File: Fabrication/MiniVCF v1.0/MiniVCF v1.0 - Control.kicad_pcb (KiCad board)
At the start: 2 copper layers, 30 x 102.5 mm, 28 parts, among them J10 CV2, J11 CTRL_PANEL_CONN2, J3 AudioIn, J4 CV1, J5 AudioOut, J6 CONN_PWR1, J9 CTRL_PANEL_CONN

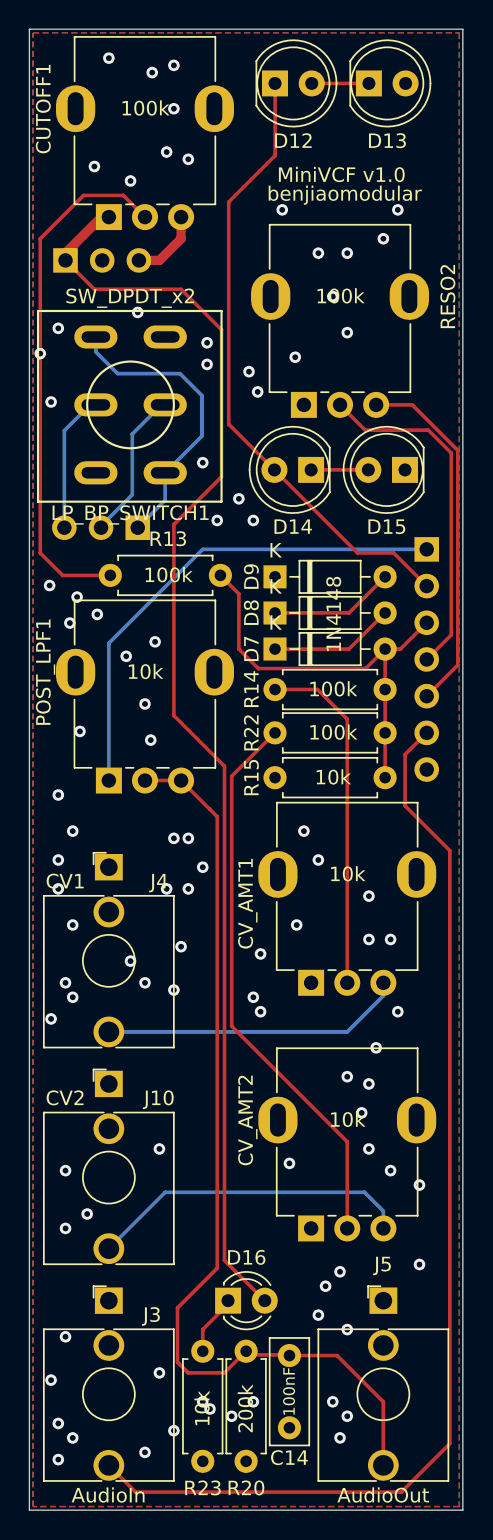
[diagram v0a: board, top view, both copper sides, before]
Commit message: Added a lock hole on control and main board
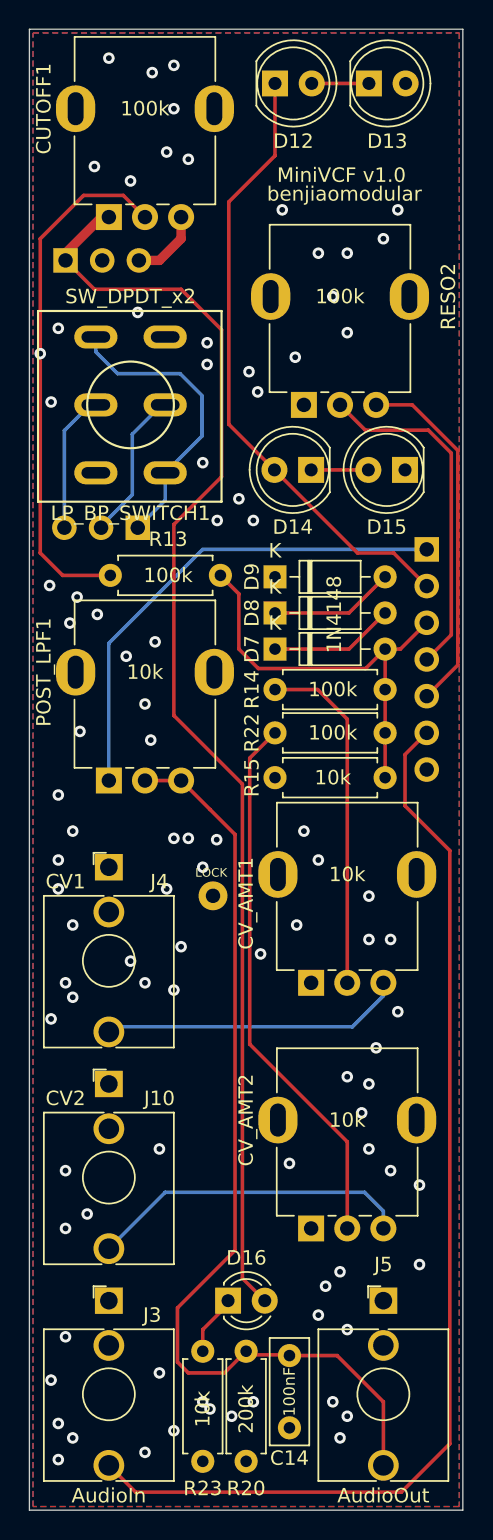
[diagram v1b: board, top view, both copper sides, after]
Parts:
- added REF**: Wire_1mm, benjiaomodular:Wire_1mm, F.Cu at (84.7, 113.0)
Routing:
- net Net-(CV_AMT2-Pad2): track 38.9 -> 37.8 mm
- net Net-(C14-Pad2): track 66.0 -> 67.0 mm
- net GND1: vias 94 -> 92
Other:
- board text added: "LOCK"
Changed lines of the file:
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@@
   (general
     (thickness 1.6)
-    (drawings 8)
-    (tracks 207)
+    (drawings 14)
+    (tracks 206)
     (zones 0)
-    (modules 28)
+    (modules 29)
     (nets 24)
   )
@@
     (add_net POS12V_1)
   )
+  (module benjiaomodular:Wire_1mm (layer F.Cu)
+    (at 84.709 113.03)
+    (fp_text reference REF** (at 0 -2) (layer F.SilkS) hide
+      (effects (font (size 1 1) (thickness 0.15)))
+    )
+    (fp_text value Wire_1mm (at 0 1.5) (layer F.Fab)
+      (effects (font (size 1 1) (thickness 0.15)))
+    )
+    (pad 1 thru_hole circle (at 0 -0.05) (size 2 2) (drill 1) (layers *.Cu *.Mask))
+  )
   (module benjiaomodular:ToggleSwitch_MTS-202_DPDT (layer F.Cu)
     (at 79 79 180)
@@
       (net 4 GND1))
   )
+  (gr_text LOCK (at 84.582 111.379) (layer B.SilkS)
+    (effects (font (size 0.6 0.6) (thickness 0.15)) (justify mirror))
+  )
+  (gr_text LOCK (at 84.582 111.379) (layer F.SilkS)
+    (effects (font (size 0.6 0.6) (thickness 0.15)))
+  )
+  (dimension 12.7 (width 0.15) (layer Dwgs.User)
+    (gr_text "12.700 mm" (at 78.359 117.632) (layer Dwgs.User)
+      (effects (font (size 1 1) (thickness 0.15)))
+    )
+    (feature1 (pts (xy 84.709 113.538) (xy 84.709 116.918421)))
+    (feature2 (pts (xy 72.009 113.538) (xy 72.009 116.918421)))
+    (crossbar (pts (xy 72.009 116.332) (xy 84.709 116.332)))
+    (arrow1a (pts (xy 84.709 116.332) (xy 83.582496 116.918421)))
+    (arrow1b (pts (xy 84.709 116.332) (xy 83.582496 115.745579)))
+    (arrow2a (pts (xy 72.009 116.332) (xy 73.135504 116.918421)))
+    (arrow2b (pts (xy 72.009 116.332) (xy 73.135504 115.745579)))
+  )
+  (dimension 15 (width 0.15) (layer Dwgs.User)
+    (gr_text "15.000 mm" (at 79.5 160.2) (layer Dwgs.User)
+      (effects (font (size 1 1) (thickness 0.15)))
+    )
+    (feature1 (pts (xy 87 141) (xy 87 159.486421)))
+    (feature2 (pts (xy 72 141) (xy 72 159.486421)))
+    (crossbar (pts (xy 72 158.9) (xy 87 158.9)))
+    (arrow1a (pts (xy 87 158.9) (xy 85.873496 159.486421)))
+    (arrow1b (pts (xy 87 158.9) (xy 85.873496 158.313579)))
+    (arrow2a (pts (xy 72 158.9) (xy 73.126504 159.486421)))
+    (arrow2b (pts (xy 72 158.9) (xy 73.126504 158.313579)))
+  )
   (dimension 10.5 (width 0.15) (layer Dwgs.User)
     (gr_text "10.500 mm" (at 96.75 139.5) (layer Dwgs.User)
@@
     (arrow2b (pts (xy 91.5 138.2) (xy 92.626504 137.613579)))
   )
+  (dimension 5.500036 (width 0.15) (layer Dwgs.User)
+    (gr_text "5.500 mm" (at 99.207077 159.293852 359.7916526) (layer Dwgs.User)
+      (effects (font (size 1 1) (thickness 0.15)))
+    )
+    (feature1 (pts (xy 102 147.5) (xy 101.959672 158.590277)))
+    (feature2 (pts (xy 96.5 147.48) (xy 96.459672 158.570277)))
+    (crossbar (pts (xy 96.461804 157.983861) (xy 101.961804 158.003861)))
+    (arrow1a (pts (xy 101.961804 158.003861) (xy 100.833175 158.586182)))
+    (arrow1b (pts (xy 101.961804 158.003861) (xy 100.83744 157.413348)))
+    (arrow2a (pts (xy 96.461804 157.983861) (xy 97.586168 158.574374)))
+    (arrow2b (pts (xy 96.461804 157.983861) (xy 97.590433 157.40154)))
+  )
   (dimension 7 (width 0.15) (layer Dwgs.User)
     (gr_text "7.000 mm" (at 75.5 84) (layer Dwgs.User)
@@
     (arrow2a (pts (xy 72 82.7) (xy 73.126504 83.286421)))
     (arrow2b (pts (xy 72 82.7) (xy 73.126504 82.113579)))
+  )
+  (dimension 5.5 (width 0.15) (layer Dwgs.User)
+    (gr_text "5.500 mm" (at 74.75 163.8) (layer Dwgs.User)
+      (effects (font (size 1 1) (thickness 0.15)))
+    )
+    (feature1 (pts (xy 72 66) (xy 72 163.086421)))
+    (feature2 (pts (xy 77.5 66) (xy 77.5 163.086421)))
+    (crossbar (pts (xy 77.5 162.5) (xy 72 162.5)))
+    (arrow1a (pts (xy 72 162.5) (xy 73.126504 161.913579)))
+    (arrow1b (pts (xy 72 162.5) (xy 73.126504 163.086421)))
+    (arrow2a (pts (xy 77.5 162.5) (xy 76.373496 161.913579)))
+    (arrow2b (pts (xy 77.5 162.5) (xy 76.373496 163.086421)))
   )
   (gr_text benjiaomodular (at 93.8 64.4) (layer F.SilkS)
@@
   (via (at 82 119.5) (size 0.8) (drill 0.4) (layers F.Cu B.Cu) (net 4))
   (via (at 82.5 116.5) (size 0.8) (drill 0.4) (layers F.Cu B.Cu) (net 4))
-  (via (at 83 112.5) (size 0.8) (drill 0.4) (layers F.Cu B.Cu) (net 4))
+  (via (at 84.963 109.093) (size 0.8) (drill 0.4) (layers F.Cu B.Cu) (net 4))
   (via (at 84 111) (size 0.8) (drill 0.4) (layers F.Cu B.Cu) (net 4))
   (via (at 83 109) (size 0.8) (drill 0.4) (layers F.Cu B.Cu) (net 4))
@@
   (via (at 90.5 115) (size 0.8) (drill 0.4) (layers F.Cu B.Cu) (net 4))
   (via (at 88 117) (size 0.8) (drill 0.4) (layers F.Cu B.Cu) (net 4))
-  (via (at 87.5 120) (size 0.8) (drill 0.4) (layers F.Cu B.Cu) (net 4))
-  (via (at 88 121) (size 0.8) (drill 0.4) (layers F.Cu B.Cu) (net 4))
   (via (at 95.5 116) (size 0.8) (drill 0.4) (layers F.Cu B.Cu) (net 4))
   (via (at 95.5 113) (size 0.8) (drill 0.4) (layers F.Cu B.Cu) (net 4))
@@
   (segment (start 79.58 69) (end 81 69) (width 0.65) (layer F.Cu) (net 5))
   (segment (start 81 69) (end 82.5 67.5) (width 0.65) (layer F.Cu) (net 5))
-  (segment (start 85.3 83.97745) (end 85.3 73.8) (width 0.25) (layer F.Cu) (net 6))
-  (segment (start 85.5 138.21) (end 85.5 104) (width 0.25) (layer F.Cu) (net 6))
-  (segment (start 88.29 141) (end 85.5 138.21) (width 0.25) (layer F.Cu) (net 6) (status 10))
-  (segment (start 82.5 71) (end 76.5 71) (width 0.25) (layer F.Cu) (net 6))
-  (segment (start 85.5 104) (end 82 100.5) (width 0.25) (layer F.Cu) (net 6))
-  (segment (start 82 100.5) (end 82 87.27745) (width 0.25) (layer F.Cu) (net 6))
-  (segment (start 82 87.27745) (end 85.3 83.97745) (width 0.25) (layer F.Cu) (net 6))
-  (segment (start 85.3 73.8) (end 82.5 71) (width 0.25) (layer F.Cu) (net 6))
-  (segment (start 76.5 71) (end 74.5 69) (width 0.25) (layer F.Cu) (net 6) (status 20))
   (segment (start 74.5 68.5) (end 74.5 69) (width 0.65) (layer F.Cu) (net 6))
   (segment (start 77.5 66) (end 77 66) (width 0.65) (layer F.Cu) (net 6))
   (segment (start 77 66) (end 74.5 68.5) (width 0.65) (layer F.Cu) (net 6))
+  (segment (start 76.5 71) (end 74.5 69) (width 0.25) (layer F.Cu) (net 6))
+  (segment (start 85.3 73.8) (end 82.5 71) (width 0.25) (layer F.Cu) (net 6))
+  (segment (start 86.741 139.451) (end 86.741 105.241) (width 0.25) (layer F.Cu) (net 6))
+  (segment (start 88.29 141) (end 86.741 139.451) (width 0.25) (layer F.Cu) (net 6))
+  (segment (start 82.5 71) (end 76.5 71) (width 0.25) (layer F.Cu) (net 6))
+  (segment (start 82 87.27745) (end 85.3 83.97745) (width 0.25) (layer F.Cu) (net 6))
+  (segment (start 85.3 83.97745) (end 85.3 73.8) (width 0.25) (layer F.Cu) (net 6))
+  (segment (start 86.741 105.241) (end 82 100.5) (width 0.25) (layer F.Cu) (net 6))
+  (segment (start 82 100.5) (end 82 87.27745) (width 0.25) (layer F.Cu) (net 6))
   (segment (start 101.64999 97.01001) (end 99.5 99.16) (width 0.25) (layer F.Cu) (net 7) (status 20))
   (segment (start 96 79) (end 98.5 79) (width 0.25) (layer F.Cu) (net 7) (status 10))
@@
   (segment (start 89 98.7) (end 91.95 98.7) (width 0.25) (layer F.Cu) (net 9))
   (segment (start 91.95 98.7) (end 94 100.75) (width 0.25) (layer F.Cu) (net 9))
+  (segment (start 77.853 122.047) (end 94.353 122.047) (width 0.25) (layer B.Cu) (net 10))
+  (segment (start 77.5 122.4) (end 77.853 122.047) (width 0.25) (layer B.Cu) (net 10))
+  (segment (start 94.353 122.047) (end 96.5 119.9) (width 0.25) (layer B.Cu) (net 10))
   (segment (start 96.5 119.9) (end 96.5 119) (width 0.25) (layer B.Cu) (net 10))
-  (segment (start 77.5 122.4) (end 94 122.4) (width 0.25) (layer B.Cu) (net 10))
-  (segment (start 94 122.4) (end 96.5 119.9) (width 0.25) (layer B.Cu) (net 10))
   (segment (start 94 130) (end 94 136) (width 0.25) (layer F.Cu) (net 11))
-  (segment (start 86 122) (end 94 130) (width 0.25) (layer F.Cu) (net 11))
-  (segment (start 89 101.7) (end 86 104.7) (width 0.25) (layer F.Cu) (net 11))
-  (segment (start 86 104.7) (end 86 122) (width 0.25) (layer F.Cu) (net 11))
+  (segment (start 87.249 123.249) (end 94 130) (width 0.25) (layer F.Cu) (net 11))
+  (segment (start 89 101.7) (end 87.249 103.451) (width 0.25) (layer F.Cu) (net 11))
+  (segment (start 87.249 103.451) (end 87.249 123.249) (width 0.25) (layer F.Cu) (net 11))
   (segment (start 96.5 134.8) (end 96.5 136) (width 0.25) (layer B.Cu) (net 12))
   (segment (start 95.2 133.5) (end 96.5 134.8) (width 0.25) (layer B.Cu) (net 12))
@@
   (segment (start 87.25 144.75) (end 89.95 144.75) (width 0.25) (layer F.Cu) (net 16) (status 30))
   (segment (start 82.5 105) (end 80 105) (width 0.25) (layer F.Cu) (net 16) (status 30))
-  (segment (start 84.5 107) (end 82.5 105) (width 0.25) (layer F.Cu) (net 16) (status 20))
-  (segment (start 85 107.5) (end 84.5 107) (width 0.25) (layer F.Cu) (net 16))
+  (segment (start 84.5 107) (end 82.5 105) (width 0.25) (layer F.Cu) (net 16))
+  (segment (start 86.233 108.733) (end 84.5 107) (width 0.25) (layer F.Cu) (net 16))
   (segment (start 85.5 146) (end 83 146) (width 0.25) (layer F.Cu) (net 16))
-  (segment (start 87 144.5) (end 85.5 146) (width 0.25) (layer F.Cu) (net 16) (status 10))
+  (segment (start 87 144.5) (end 85.5 146) (width 0.25) (layer F.Cu) (net 16))
   (segment (start 83 146) (end 82.25 145.25) (width 0.25) (layer F.Cu) (net 16))
-  (segment (start 82.25 141.5) (end 85 138.75) (width 0.25) (layer F.Cu) (net 16))
   (segment (start 82.25 145.25) (end 82.25 141.5) (width 0.25) (layer F.Cu) (net 16))
-  (segment (start 85 138.75) (end 85 107.5) (width 0.25) (layer F.Cu) (net 16))
+  (segment (start 86.233 137.517) (end 86.233 108.733) (width 0.25) (layer F.Cu) (net 16))
+  (segment (start 82.25 141.5) (end 86.233 137.517) (width 0.25) (layer F.Cu) (net 16))
   (segment (start 97.68 95.9) (end 96.62 95.9) (width 0.25) (layer F.Cu) (net 17) (status 20))
   (segment (start 99.5 94.08) (end 97.68 95.9) (width 0.25) (layer F.Cu) (net 17) (status 10))
